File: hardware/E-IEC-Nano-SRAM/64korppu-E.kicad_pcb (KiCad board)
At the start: 2 copper layers, 85 x 55 mm, 27 parts, among them J1 DIN-6_IEC, J2 Floppy_34pin, J3 DC_Jack, U1 Arduino_Nano, U2 23LC1024, U3 74HC595

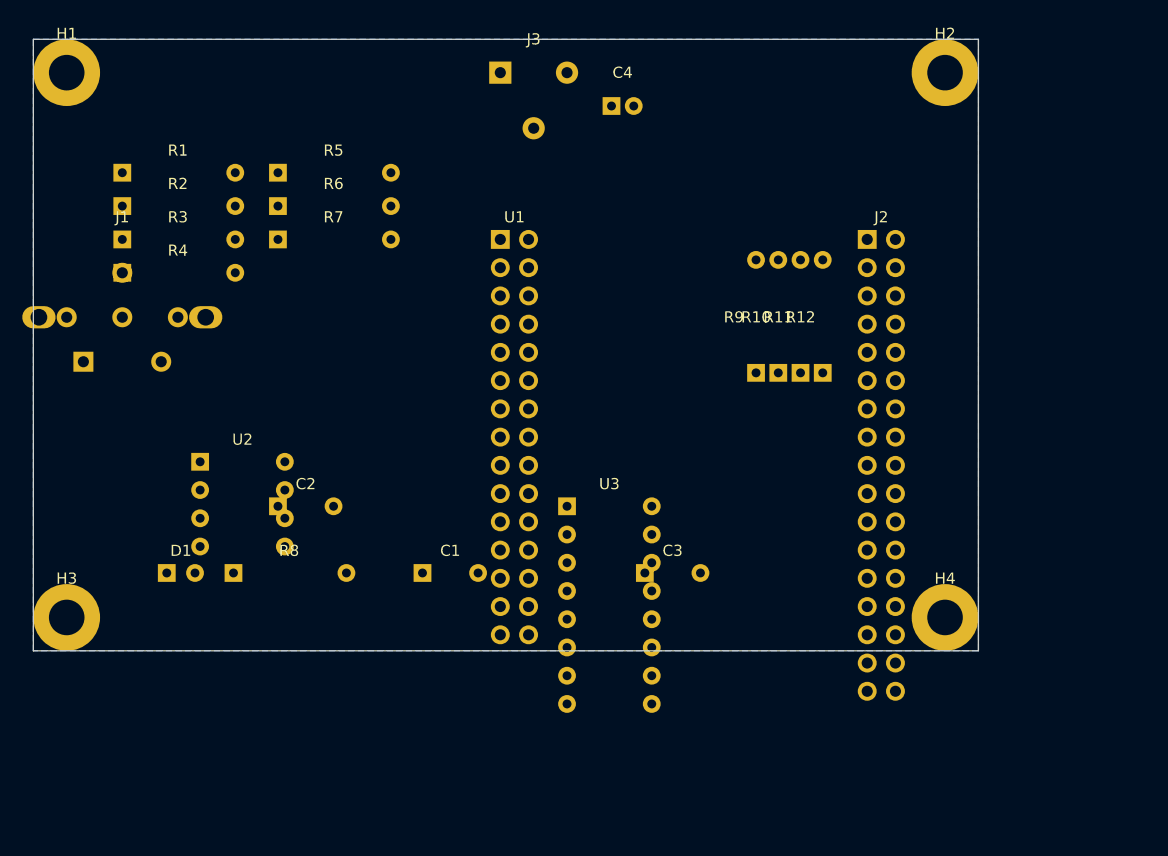
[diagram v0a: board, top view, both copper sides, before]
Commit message: fix(hw): enlarge PCB to 100x70mm and spread components for routing
Co-Authored-By: Claude Opus 4.6 <noreply@anthropic.com>
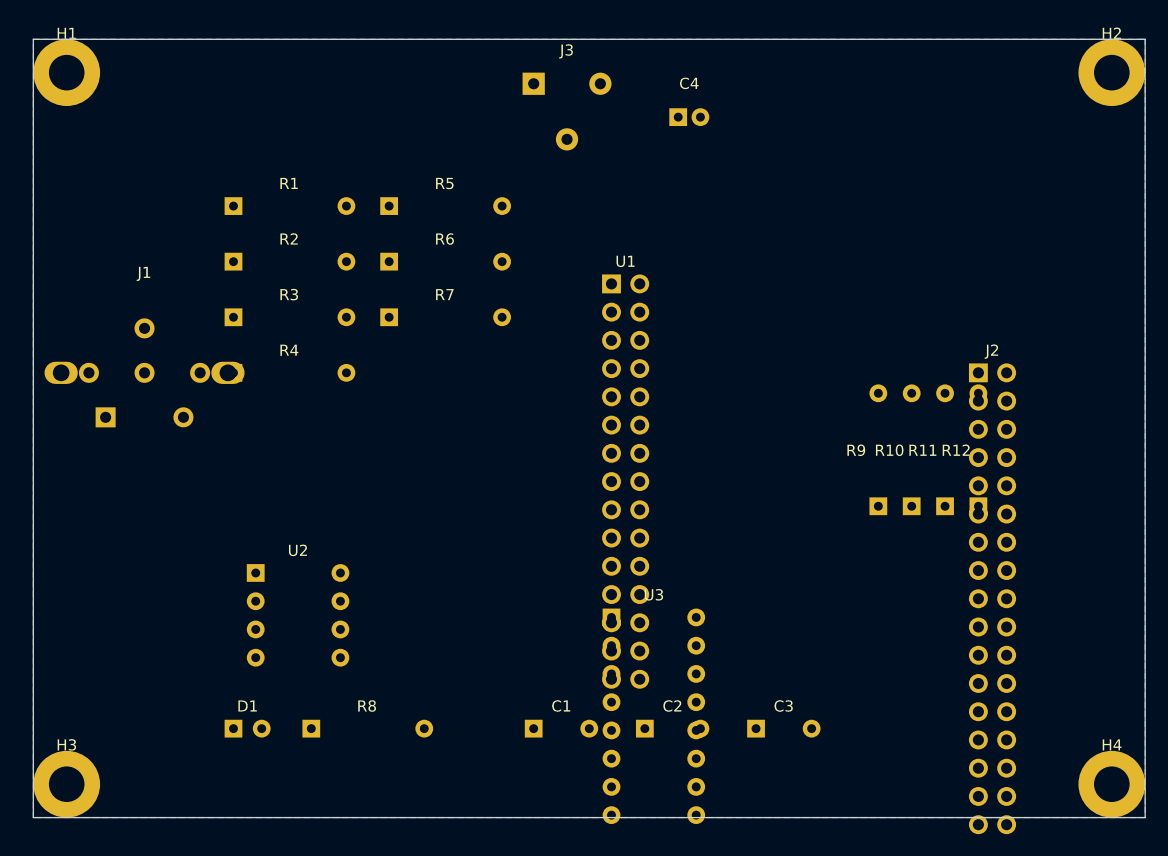
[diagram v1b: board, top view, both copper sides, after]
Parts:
- moved C2 38.6 mm to (155.0, 162.0)
- moved H4 21.2 mm to (197.0, 167.0)
- moved R12 18.4 mm to (185.0, 142.0)
- moved R11 17.7 mm to (182.0, 142.0)
- moved C1 17.2 mm to (145.0, 162.0)
- moved C3 17.2 mm to (165.0, 162.0)
- moved R10 17.0 mm to (179.0, 142.0)
- moved R9 16.3 mm to (176.0, 142.0)
- moved R8 15.7 mm to (125.0, 162.0)
- moved J2 15.6 mm to (185.0, 130.0)
- moved D1 15.2 mm to (118.0, 162.0)
- moved H2 15.0 mm to (197.0, 103.0)
- moved H3 15.0 mm to (103.0, 167.0)
- moved R4 13.5 mm to (118.0, 130.0)
- moved R3 12.2 mm to (118.0, 125.0)
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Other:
- board size 85 x 55 mm -> 100 x 70 mm
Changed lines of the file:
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@@
 	(footprint "Connector_BarrelJack:BarrelJack_Horizontal"
 		(layer "F.Cu")
-		(at 142 103)
+		(at 145 104)
 		(property "Reference" "J3"
 			(at 3 -3 0)
@@
 	(footprint "Capacitor_THT:CP_Radial_D5.0mm_P2.00mm"
 		(layer "F.Cu")
-		(at 152 106)
+		(at 158 107)
 		(property "Reference" "C4"
 			(at 1 -3 0)
@@
 	(footprint "64korppu-E:DIN-6_IEC_Vertical"
 		(layer "F.Cu")
-		(at 108 125)
+		(at 110 130)
 		(property "Reference" "J1"
 			(at 0 -9 0)
@@
 	(footprint "Resistor_THT:R_Axial_DIN0207_L6.3mm_D2.5mm_P10.16mm_Horizontal"
 		(layer "F.Cu")
-		(at 108 112)
+		(at 118 115)
 		(property "Reference" "R1"
 			(at 5 -2 0)
@@
 	(footprint "Resistor_THT:R_Axial_DIN0207_L6.3mm_D2.5mm_P10.16mm_Horizontal"
 		(layer "F.Cu")
-		(at 108 115)
+		(at 118 120)
 		(property "Reference" "R2"
 			(at 5 -2 0)
@@
 	(footprint "Resistor_THT:R_Axial_DIN0207_L6.3mm_D2.5mm_P10.16mm_Horizontal"
 		(layer "F.Cu")
-		(at 108 118)
+		(at 118 125)
 		(property "Reference" "R3"
 			(at 5 -2 0)
@@
 	(footprint "Resistor_THT:R_Axial_DIN0207_L6.3mm_D2.5mm_P10.16mm_Horizontal"
 		(layer "F.Cu")
-		(at 108 121)
+		(at 118 130)
 		(property "Reference" "R4"
 			(at 5 -2 0)
@@
 	(footprint "Resistor_THT:R_Axial_DIN0207_L6.3mm_D2.5mm_P10.16mm_Horizontal"
 		(layer "F.Cu")
-		(at 122 112)
+		(at 132 115)
 		(property "Reference" "R5"
 			(at 5 -2 0)
@@
 	(footprint "Resistor_THT:R_Axial_DIN0207_L6.3mm_D2.5mm_P10.16mm_Horizontal"
 		(layer "F.Cu")
-		(at 122 115)
+		(at 132 120)
 		(property "Reference" "R6"
 			(at 5 -2 0)
@@
 	(footprint "Resistor_THT:R_Axial_DIN0207_L6.3mm_D2.5mm_P10.16mm_Horizontal"
 		(layer "F.Cu")
-		(at 122 118)
+		(at 132 125)
 		(property "Reference" "R7"
 			(at 5 -2 0)
@@
 	(footprint "Connector_PinHeader_2.54mm:PinHeader_2x15_P2.54mm_Vertical"
 		(layer "F.Cu")
-		(at 142 118)
+		(at 152 122)
 		(property "Reference" "U1"
 			(at 1.27 -2 0)
@@
 	(footprint "Package_DIP:DIP-8_W7.62mm_Socket"
 		(layer "F.Cu")
-		(at 115 138)
+		(at 120 148)
 		(property "Reference" "U2"
 			(at 3.81 -2 0)
@@
 	(footprint "Package_DIP:DIP-16_W7.62mm_Socket"
 		(layer "F.Cu")
-		(at 148 142)
+		(at 152 152)
 		(property "Reference" "U3"
 			(at 3.81 -2 0)
@@
 	(footprint "Connector_IDC:IDC-Header_2x17_P2.54mm_Vertical"
 		(layer "F.Cu")
-		(at 175 118)
+		(at 185 130)
 		(property "Reference" "J2"
 			(at 1.27 -2 0)
@@
 	(footprint "Resistor_THT:R_Axial_DIN0207_L6.3mm_D2.5mm_P10.16mm_Horizontal"
 		(layer "F.Cu")
-		(at 118 148)
+		(at 125 162)
 		(property "Reference" "R8"
 			(at 5 -2 0)
@@
 	(footprint "LED_THT:LED_D3.0mm"
 		(layer "F.Cu")
-		(at 112 148)
+		(at 118 162)
 		(property "Reference" "D1"
 			(at 1.27 -2 0)
@@
 	(footprint "Resistor_THT:R_Axial_DIN0207_L6.3mm_D2.5mm_P10.16mm_Horizontal"
 		(layer "F.Cu")
-		(at 165 130 90)
+		(at 176 142 90)
 		(property "Reference" "R9"
 			(at 5 -2 0)
@@
 	(footprint "Resistor_THT:R_Axial_DIN0207_L6.3mm_D2.5mm_P10.16mm_Horizontal"
 		(layer "F.Cu")
-		(at 167 130 90)
+		(at 179 142 90)
 		(property "Reference" "R10"
 			(at 5 -2 0)
@@
 	(footprint "Resistor_THT:R_Axial_DIN0207_L6.3mm_D2.5mm_P10.16mm_Horizontal"
 		(layer "F.Cu")
-		(at 169 130 90)
+		(at 182 142 90)
 		(property "Reference" "R11"
 			(at 5 -2 0)
@@
 	(footprint "Resistor_THT:R_Axial_DIN0207_L6.3mm_D2.5mm_P10.16mm_Horizontal"
 		(layer "F.Cu")
-		(at 171 130 90)
+		(at 185 142 90)
 		(property "Reference" "R12"
 			(at 5 -2 0)
@@
 	(footprint "Capacitor_THT:C_Disc_D5.0mm_W2.5mm_P5.00mm"
 		(layer "F.Cu")
-		(at 135 148)
+		(at 145 162)
 		(property "Reference" "C1"
 			(at 2.5 -2 0)
@@
 	(footprint "Capacitor_THT:C_Disc_D5.0mm_W2.5mm_P5.00mm"
 		(layer "F.Cu")
-		(at 122 142)
+		(at 155 162)
 		(property "Reference" "C2"
 			(at 2.5 -2 0)
@@
 	(footprint "Capacitor_THT:C_Disc_D5.0mm_W2.5mm_P5.00mm"
 		(layer "F.Cu")
-		(at 155 148)
+		(at 165 162)
 		(property "Reference" "C3"
 			(at 2.5 -2 0)
@@
 	(footprint "MountingHole:MountingHole_3.2mm_M3"
 		(layer "F.Cu")
-		(at 182 103)
+		(at 197 103)
 		(property "Reference" "H2"
 			(at 0 -3.5 0)
@@
 	(footprint "MountingHole:MountingHole_3.2mm_M3"
 		(layer "F.Cu")
-		(at 103 152)
+		(at 103 167)
 		(property "Reference" "H3"
 			(at 0 -3.5 0)
@@
 	(footprint "MountingHole:MountingHole_3.2mm_M3"
 		(layer "F.Cu")
-		(at 182 152)
+		(at 197 167)
 		(property "Reference" "H4"
 			(at 0 -3.5 0)
@@
 	(gr_rect
 		(start 100 100)
-		(end 185 155)
+		(end 200 170)
 		(stroke
 			(width 0.05)
@@
 			(pts
 				(xy 100 100)
-				(xy 185 100)
-				(xy 185 155)
-				(xy 100 155)
-			)
-		)
+				(xy 200 100)
+				(xy 200 170)
+				(xy 100 170)
+			)
+		)

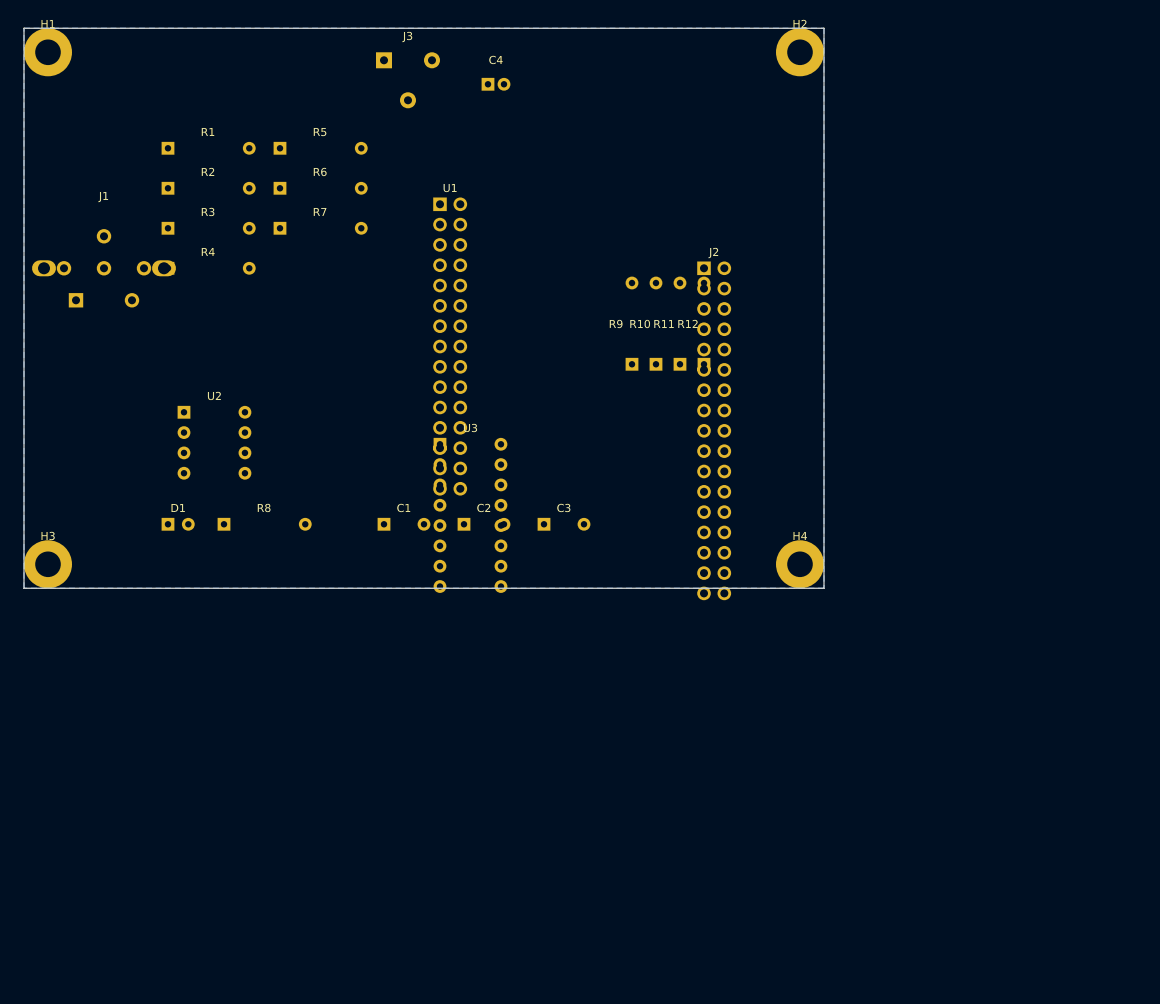
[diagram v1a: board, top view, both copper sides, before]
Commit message: Add Gerber zip to bin/E-IEC-Nano-SRAM and fix PCB layout
Move firmware binary and add manufacturing Gerbers into
bin/E-IEC-Nano-SRAM/. Fix PCB: move R9-R12 and U3 to
eliminate pad overlaps, enlarge board to 115x95mm, fill
GND zone. All 30 nets routed by Freerouting.

Co-Authored-By: Claude Opus 4.6 <noreply@anthropic.com>
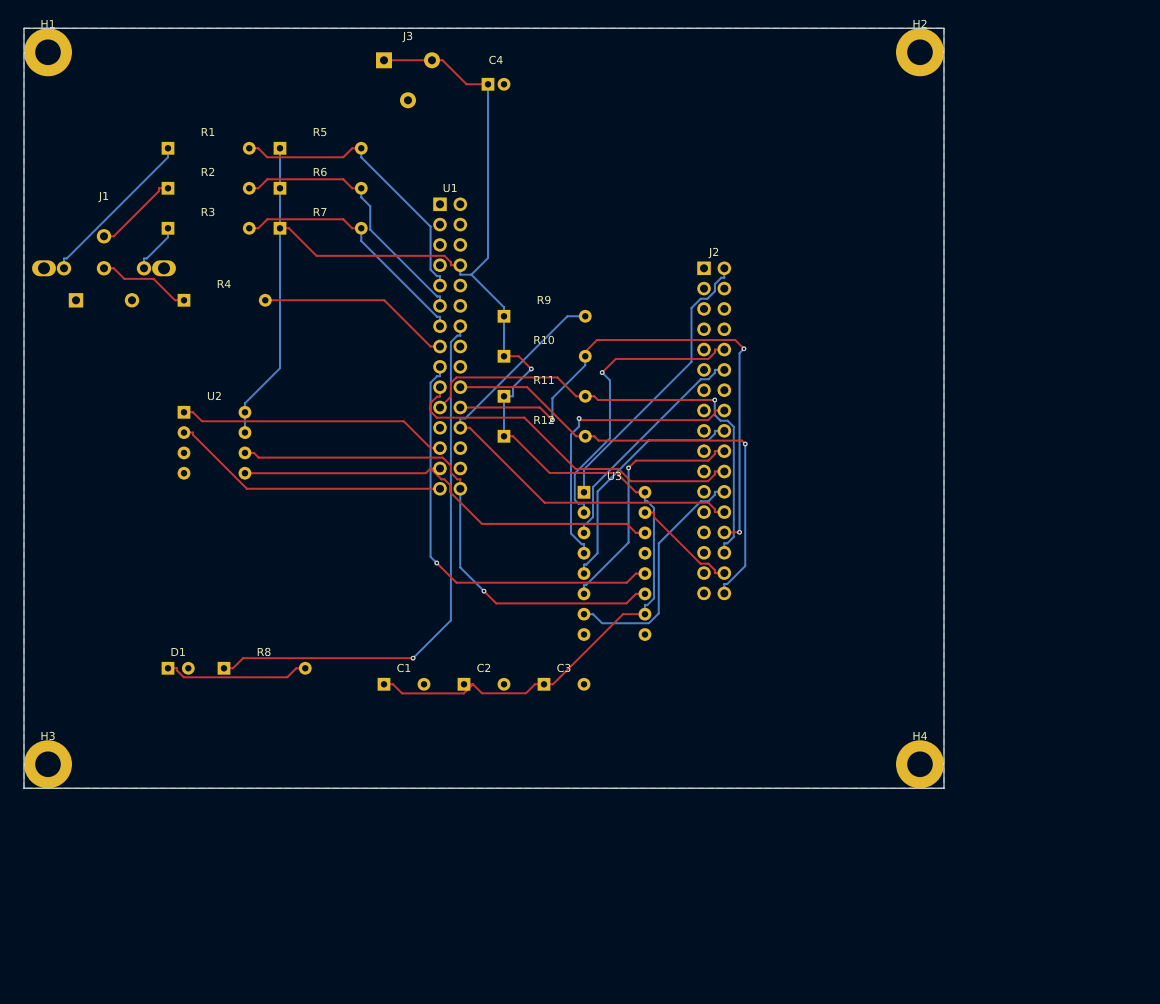
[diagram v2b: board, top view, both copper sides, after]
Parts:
- moved H4 29.2 mm to (212.0, 192.0)
- moved R12 26.6 mm to (160.0, 151.0), turned to 0 degrees
- moved H3 25.0 mm to (103.0, 192.0)
- moved R11 22.4 mm to (160.0, 146.0), turned to 0 degrees
- moved C1 20.0 mm to (145.0, 182.0)
- moved C2 20.0 mm to (155.0, 182.0)
- moved C3 20.0 mm to (165.0, 182.0)
- moved R10 19.0 mm to (160.0, 141.0), turned to 0 degrees
- moved U3 19.0 mm to (170.0, 158.0)
- moved D1 18.0 mm to (118.0, 180.0)
- moved R8 18.0 mm to (125.0, 180.0)
- moved R9 17.1 mm to (160.0, 136.0), turned to 0 degrees
- moved H2 15.0 mm to (212.0, 103.0)
- moved R4 4.47 mm to (120.0, 134.0)
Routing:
- net +5V: track 0.00 -> 206.2 mm, vias 0 -> 1
- net FLOPPY_WPT: track 0.00 -> 69.2 mm, vias 0 -> 3
- net LED_ANODE: track 0.00 -> 68.3 mm, vias 0 -> 1
- net SPI_SCK: track 0.00 -> 65.3 mm, vias 0 -> 1
- net FLOPPY_TRK00: track 0.00 -> 59.7 mm
- net FLOPPY_RDATA: track 0.00 -> 59.4 mm, vias 0 -> 1
- net FLOPPY_DSKCHG: track 0.00 -> 58.5 mm, vias 0 -> 1
- net SPI_MOSI: track 0.00 -> 55.3 mm
- net LATCH_595: track 0.00 -> 53.1 mm, vias 0 -> 1
- net FLOPPY_WDATA: track 0.00 -> 44.8 mm
- net FLOPPY_MOTEA: track 0.00 -> 37.3 mm, vias 0 -> 1
- net FLOPPY_MOTOR: track 0.00 -> 37.1 mm, vias 0 -> 1
- net NANO_D2: track 0.00 -> 36.4 mm
- net FLOPPY_DENSITY: track 0.00 -> 36.0 mm
- net SPI_MISO: track 0.00 -> 35.1 mm
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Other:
- board size 100 x 70 mm -> 115 x 95 mm

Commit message: Geometric PCB layout with aligned components and fix grep -P for macOS
- Redesign component placement with grid-aligned positions
- Power row at y=108, ICs at y=172, passives at y=198
- Consistent 7-8mm spacing between resistor groups
- Fix pcb-pipeline.sh grep -P (PCRE) to sed for macOS compatibility
- Update gerber zip in bin/

Co-Authored-By: Claude Opus 4.6 <noreply@anthropic.com>
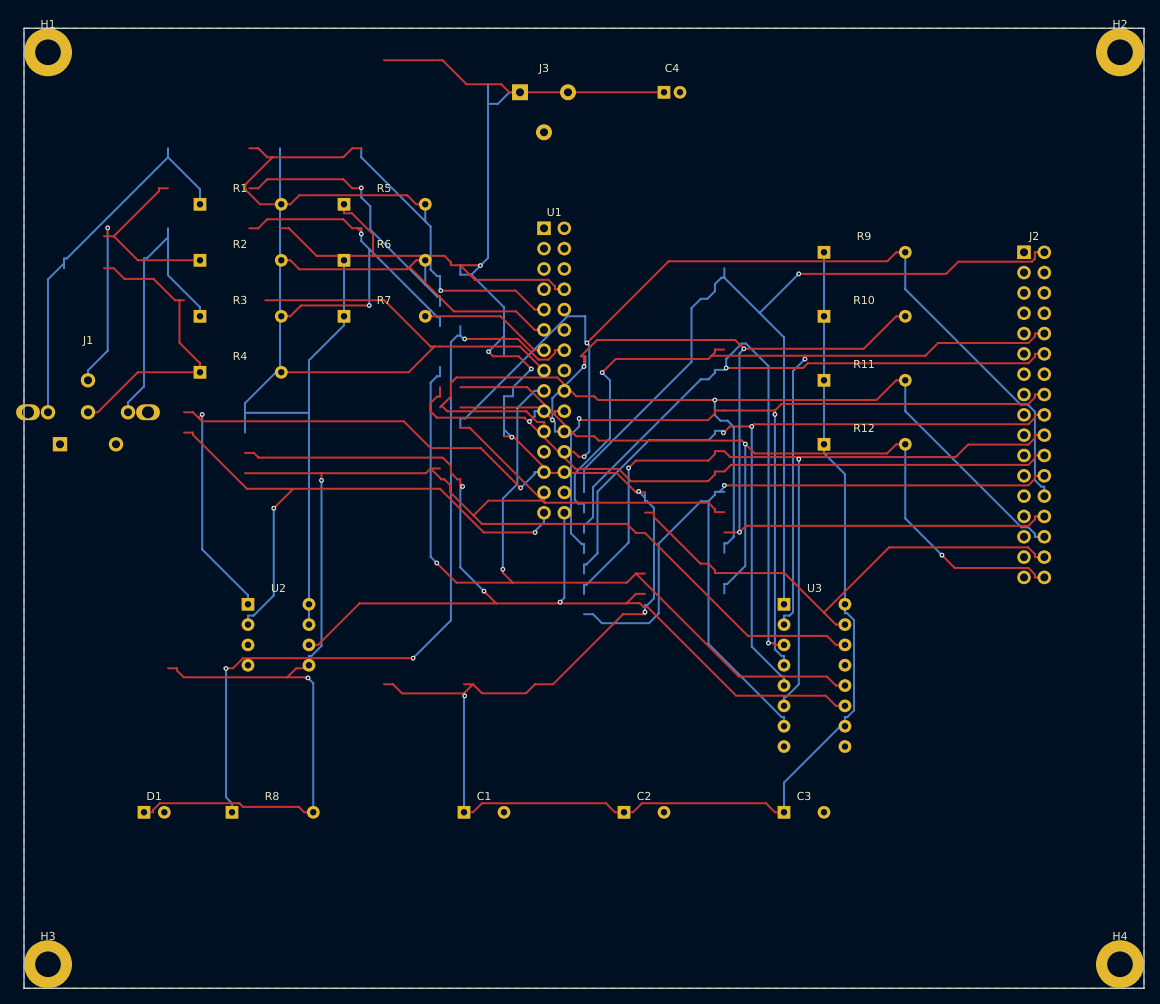
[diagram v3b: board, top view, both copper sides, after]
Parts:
- moved R9 40.8 mm to (200.0, 128.0)
- moved R10 40.3 mm to (200.0, 136.0)
- moved J2 40.0 mm to (225.0, 128.0)
- moved R11 40.0 mm to (200.0, 144.0)
- moved R12 40.0 mm to (200.0, 152.0)
- moved H4 35.4 mm to (237.0, 217.0)
- moved C3 34.0 mm to (195.0, 198.0)
- moved U3 28.7 mm to (195.0, 172.0)
- moved C2 25.6 mm to (175.0, 198.0)
- moved U2 25.3 mm to (128.0, 172.0)
- moved H2 25.0 mm to (237.0, 103.0)
- moved H3 25.0 mm to (103.0, 217.0)
- moved C4 22.0 mm to (180.0, 108.0)
- moved C1 18.9 mm to (155.0, 198.0)
- moved D1 18.2 mm to (115.0, 198.0)
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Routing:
- net +5V: track 206.2 -> 457.0 mm, vias 1 -> 7
- net SPI_MOSI: track 55.3 -> 159.2 mm, vias 0 -> 1
- net FLOPPY_DRVSEL: track 29.1 -> 115.1 mm, vias 0 -> 2
- net FLOPPY_DENSITY: track 36.0 -> 119.1 mm, vias 0 -> 1
- net FLOPPY_MOTEA: track 37.3 -> 115.3 mm, vias 1 -> 2
- net FLOPPY_DIR: track 30.3 -> 106.2 mm, vias 0 -> 2
- net FLOPPY_WGATE: track 30.1 -> 104.1 mm, vias 0 -> 1
- net FLOPPY_STEP: track 31.3 -> 105.0 mm, vias 1 -> 2
- net FLOPPY_MOTOR: track 37.1 -> 110.6 mm, vias 1 -> 2
- net SPI_SCK: track 65.3 -> 135.9 mm, vias 1 -> 3
- net FLOPPY_RDATA: track 59.4 -> 127.0 mm
- net FLOPPY_TRK00: track 59.7 -> 125.7 mm, vias 0 -> 2
- net FLOPPY_WPT: track 69.2 -> 134.2 mm, vias 3 -> 4
- net LATCH_595: track 53.1 -> 112.3 mm, vias 1 -> 2
- net FLOPPY_DSKCHG: track 58.5 -> 111.0 mm, vias 1 -> 2
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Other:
- board size 115 x 95 mm -> 140 x 120 mm
